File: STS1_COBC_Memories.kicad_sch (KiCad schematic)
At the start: 7 parts, among them J5 Flash_Dbg, U1 W25Q01JVZEIQ, U17 CY15B108QN-40SXI

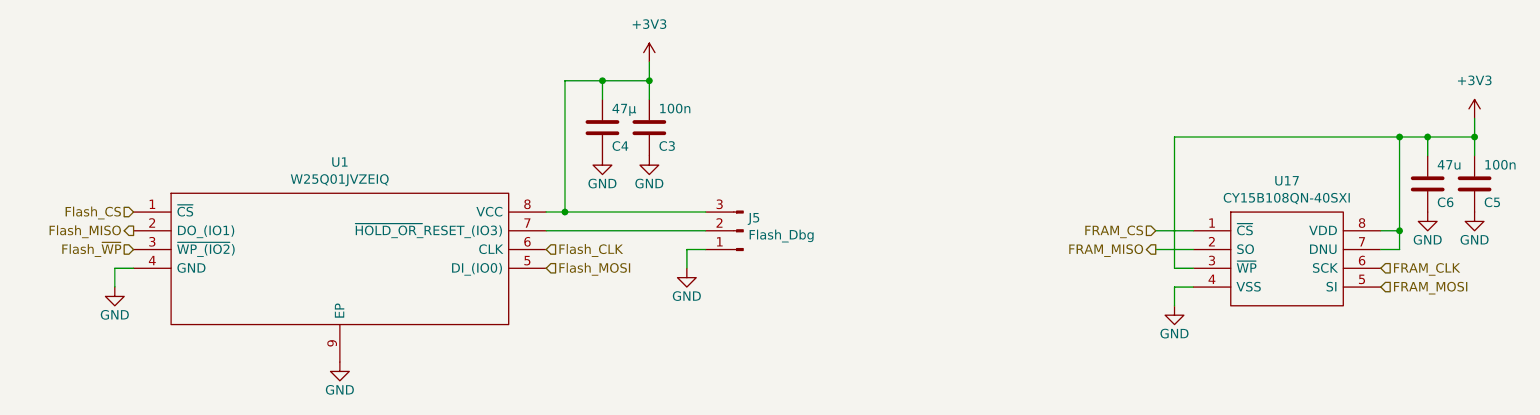
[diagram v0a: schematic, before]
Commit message: Fix footprint assignments: all CSBI headers should have J designator
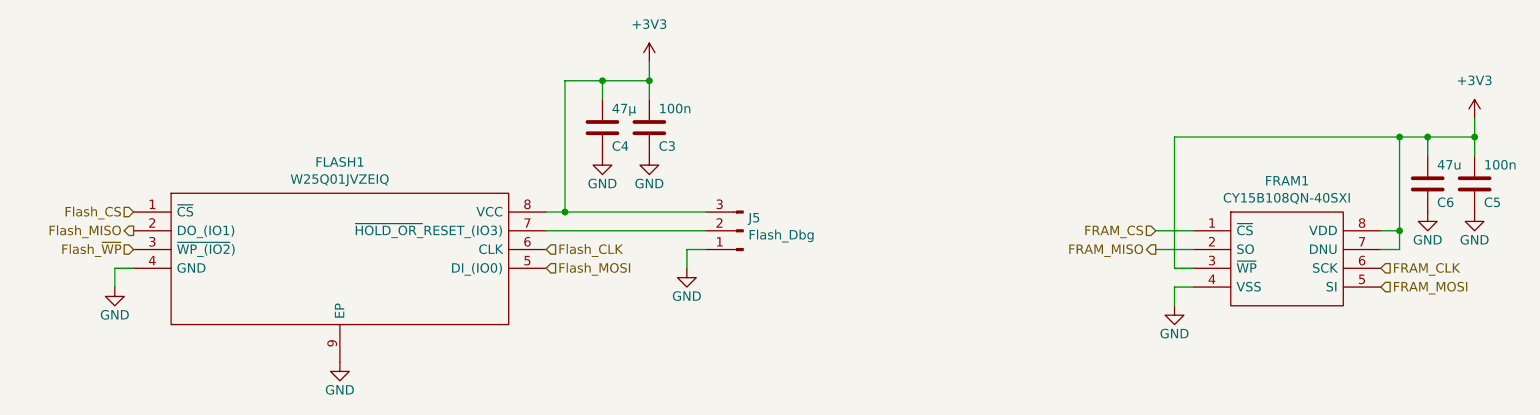
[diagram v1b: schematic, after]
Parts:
- renumbered U1 to FLASH1, U17 to FRAM1
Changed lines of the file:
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@@
   (symbol (lib_id "STS1_COBC_V2-rescue:W25Q01JVZEIQ-W25Q01JVZEIQ") (at 53.34 71.12 0) (unit 1)
     (in_bom yes) (on_board yes)
-    (property "Reference" "U1" (id 0) (at 81.28 64.389 0))
+    (property "Reference" "FLASH1" (id 0) (at 81.28 64.389 0))
     (property "Value" "W25Q01JVZEIQ" (id 1) (at 81.28 66.7004 0))
     (property "Footprint" "STSLib:SON127P800X600X80-9N-D" (id 2) (at 105.41 68.58 0)
@@
   (symbol (lib_id "STS1_COBC_V2-rescue:CY15B108QN-40SXI-CY15B108QN-40SXI") (at 196.85 73.66 0) (unit 1)
     (in_bom yes) (on_board yes)
-    (property "Reference" "U17" (id 0) (at 209.55 66.929 0))
+    (property "Reference" "FRAM1" (id 0) (at 209.55 66.929 0))
     (property "Value" "CY15B108QN-40SXI" (id 1) (at 209.55 69.2404 0))
     (property "Footprint" "STSLib:SOIC127P800X203-8N" (id 2) (at 218.44 71.12 0)
